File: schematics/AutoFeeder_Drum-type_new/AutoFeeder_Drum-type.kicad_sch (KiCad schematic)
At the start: 44 parts, among them J1 USB_C_Receptacle_6, J2 Conn_01x04, J3 Conn_01x05, J4 Conn_02x02_Odd_Even, J5 Conn_01x04, J6 Conn_02x02_Odd_Even, J7 Conn_01x04, J8 Conn_01x03, J9 Conn_01x04, M1 Motor_DC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

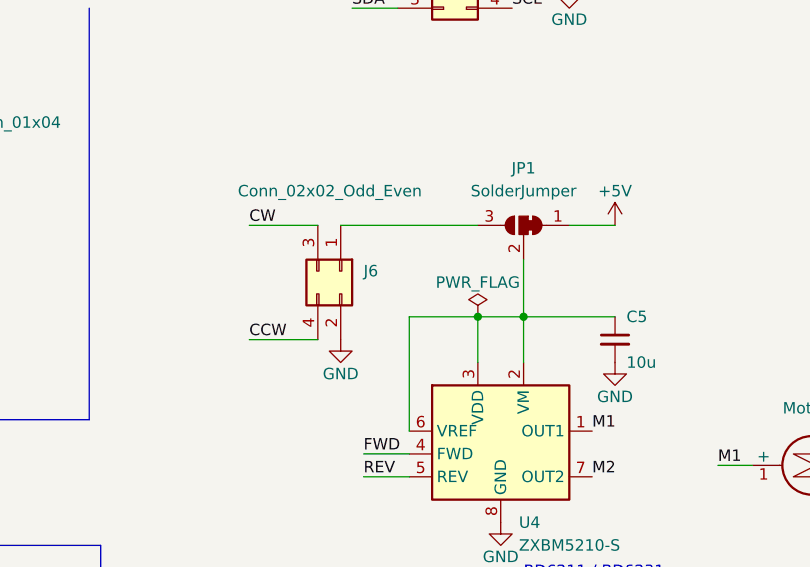
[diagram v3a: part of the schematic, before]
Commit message: Schematics: Add +5V to J6; Fine-tuning of patterns
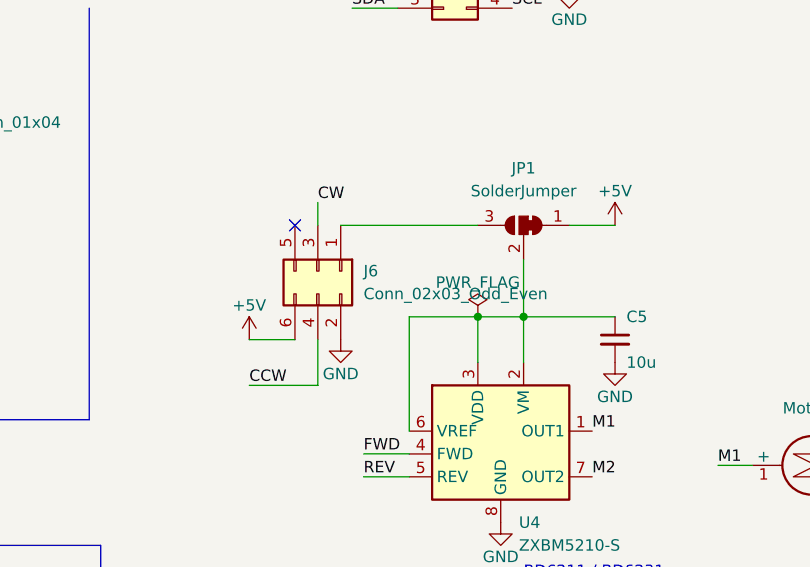
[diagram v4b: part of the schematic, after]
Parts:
- removed J6: Conn_02x02_Odd_Even, Connector_PinHeader_2.54mm:PinHeader_2x02_P2.54mm_Vertical, symbol Connector_Generic:Conn_02x02_Odd_Even
- added J6: Conn_02x03_Odd_Even, Connector_PinHeader_2.54mm:PinHeader_2x03_P2.54mm_Vertical, symbol Connector_Generic:Conn_02x03_Odd_Even
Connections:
- net +5V: now also J6.6 (Pin_6)
- net CCW: now also J6.4 (Pin_4)
- net CW: now also J6.3 (Pin_3)
- net GND: now also J6.2 (Pin_2)
- net at JP1.3 (B): now also J6.1 (Pin_1)
- no-connect marks 8 -> 9
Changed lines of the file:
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@@
   (no_connect (at 139.7 166.37))
   (no_connect (at 99.06 34.29))
+  (no_connect (at 193.04 121.92))
   (no_connect (at 118.11 26.67))
   (no_connect (at 99.06 39.37))
@@
     (stroke (width 0) (type default) (color 0 0 0 0))
   )
+  (wire (pts (xy 195.58 119.38) (xy 195.58 121.92))
+    (stroke (width 0) (type default) (color 0 0 0 0))
+  )
   (wire (pts (xy 228.6 121.92) (xy 223.52 121.92))
     (stroke (width 0) (type default) (color 0 0 0 0))
@@
     (stroke (width 0) (type default) (color 0 0 0 0))
   )
-  (wire (pts (xy 187.96 134.62) (xy 195.58 134.62))
+  (wire (pts (xy 187.96 139.7) (xy 195.58 139.7))
     (stroke (width 0) (type default) (color 0 0 0 0))
   )
@@
     (stroke (width 0) (type default) (color 0 0 0 0))
   )
+  (wire (pts (xy 195.58 134.62) (xy 195.58 139.7))
+    (stroke (width 0) (type default) (color 0 0 0 0))
+  )
   (wire (pts (xy 38.1 115.57) (xy 38.1 118.11))
     (stroke (width 0) (type default) (color 0 0 0 0))
@@
     (stroke (width 0) (type solid) (color 0 0 0 0))
   )
-  (wire (pts (xy 187.96 121.92) (xy 195.58 121.92))
-    (stroke (width 0) (type default) (color 0 0 0 0))
-  )
   (wire (pts (xy 198.12 72.39) (xy 205.74 72.39))
     (stroke (width 0) (type default) (color 0 0 0 0))
@@
   (polyline (pts (xy 90.17 62.23) (xy 91.44 59.69))
     (stroke (width 0) (type solid) (color 0 0 255 1))
+  )
+  (wire (pts (xy 187.96 134.62) (xy 193.04 134.62))
+    (stroke (width 0) (type default) (color 0 0 0 0))
   )
   (wire (pts (xy 38.1 118.11) (xy 43.18 118.11))
@@
     (effects (font (size 1.27 1.27)) (justify left bottom))
   )
-  (label "CW" (at 187.96 121.92 0)
+  (label "CW" (at 195.58 119.38 0)
     (effects (font (size 1.27 1.27)) (justify left bottom))
   )
@@
     (effects (font (size 1.27 1.27)) (justify left bottom))
   )
-  (label "CCW" (at 187.96 134.62 0)
+  (label "CCW" (at 187.96 139.7 0)
     (effects (font (size 1.27 1.27)) (justify left bottom))
   )
@@
   (label "Sensor0" (at 260.35 74.93 0)
     (effects (font (size 1.27 1.27)) (justify left bottom))
-  )
-  (symbol (lib_id "Connector_Generic:Conn_02x02_Odd_Even") (at 198.12 127 270) (unit 1)
-    (in_bom yes) (on_board yes)
-    (property "Reference" "J6" (id 0) (at 200.66 126.9999 90)
-      (effects (font (size 1.27 1.27)) (justify left))
-    )
-    (property "Value" "Conn_02x02_Odd_Even" (id 1) (at 186.69 118.11 90)
-      (effects (font (size 1.27 1.27)) (justify left))
-    )
-    (property "Footprint" "Connector_PinHeader_2.54mm:PinHeader_2x02_P2.54mm_Vertical" (id 2) (at 198.12 127 0)
-      (effects (font (size 1.27 1.27)) hide)
-    )
-    (property "Datasheet" "~" (id 3) (at 198.12 127 0)
-      (effects (font (size 1.27 1.27)) hide)
-    )
-    (pin "1")
-    (pin "2")
-    (pin "3")
-    (pin "4")
   )
   (symbol (lib_id "Device:R") (at 107.95 105.41 270) (unit 1)
@@
     (pin "1")
   )
-  (symbol (lib_id "mylib1:SW_PUSH_DPDT_x2") (at 251.46 64.77 0) (unit 2)
-    (in_bom yes) (on_board yes) (fields_autoplaced)
-    (property "Reference" "SW3" (id 0) (at 251.46 57.15 0))
-    (property "Value" "IS-2235" (id 1) (at 251.46 59.69 0))
-    (property "Footprint" "mylib:Slide-SW-IS-2235" (id 2) (at 251.46 64.77 0)
-      (effects (font (size 1.27 1.27)) hide)
-    )
-    (property "Datasheet" "" (id 3) (at 251.46 64.77 0)
+  (symbol (lib_id "Connector_Generic:Conn_02x03_Odd_Even") (at 195.58 127 270) (unit 1)
+    (in_bom yes) (on_board yes) (fields_autoplaced)
+    (property "Reference" "J6" (id 0) (at 200.66 126.9999 90)
+      (effects (font (size 1.27 1.27)) (justify left))
+    )
+    (property "Value" "Conn_02x03_Odd_Even" (id 1) (at 200.66 129.5399 90)
+      (effects (font (size 1.27 1.27)) (justify left))
+    )
+    (property "Footprint" "Connector_PinHeader_2.54mm:PinHeader_2x03_P2.54mm_Vertical" (id 2) (at 195.58 127 0)
+      (effects (font (size 1.27 1.27)) hide)
+    )
+    (property "Datasheet" "~" (id 3) (at 195.58 127 0)
       (effects (font (size 1.27 1.27)) hide)
     )
@@
     (pin "6")
   )
-  (symbol (lib_id "mylib1:SW_PUSH_DPDT_x2") (at 123.19 36.83 0) (mirror y) (unit 1)
-    (in_bom yes) (on_board yes) (fields_autoplaced)
-    (property "Reference" "SW2" (id 0) (at 123.19 29.21 0))
-    (property "Value" "IS-2235" (id 1) (at 123.19 31.75 0))
-    (property "Footprint" "mylib:Slide-SW-IS-2235" (id 2) (at 123.19 36.83 0)
-      (effects (font (size 1.27 1.27)) hide)
-    )
-    (property "Datasheet" "" (id 3) (at 123.19 36.83 0)
+  (symbol (lib_id "mylib1:SW_PUSH_DPDT_x2") (at 251.46 64.77 0) (unit 2)
+    (in_bom yes) (on_board yes) (fields_autoplaced)
+    (property "Reference" "SW3" (id 0) (at 251.46 57.15 0))
+    (property "Value" "IS-2235" (id 1) (at 251.46 59.69 0))
+    (property "Footprint" "mylib:Slide-SW-IS-2235" (id 2) (at 251.46 64.77 0)
+      (effects (font (size 1.27 1.27)) hide)
+    )
+    (property "Datasheet" "" (id 3) (at 251.46 64.77 0)
       (effects (font (size 1.27 1.27)) hide)
     )
@@
     (pin "6")
   )
+  (symbol (lib_id "mylib1:SW_PUSH_DPDT_x2") (at 123.19 36.83 0) (mirror y) (unit 1)
+    (in_bom yes) (on_board yes) (fields_autoplaced)
+    (property "Reference" "SW2" (id 0) (at 123.19 29.21 0))
+    (property "Value" "IS-2235" (id 1) (at 123.19 31.75 0))
+    (property "Footprint" "mylib:Slide-SW-IS-2235" (id 2) (at 123.19 36.83 0)
+      (effects (font (size 1.27 1.27)) hide)
+    )
+    (property "Datasheet" "" (id 3) (at 123.19 36.83 0)
+      (effects (font (size 1.27 1.27)) hide)
+    )
+    (pin "1")
+    (pin "2")
+    (pin "3")
+    (pin "4")
+    (pin "5")
+    (pin "6")
+  )
   (symbol (lib_id "Device:R") (at 100.33 180.34 0) (unit 1)
     (in_bom yes) (on_board yes)
@@
     )
     (property "Datasheet" "~" (id 3) (at 43.18 118.11 0)
+      (effects (font (size 1.27 1.27)) hide)
+    )
+    (pin "1")
+  )
+  (symbol (lib_id "power:+5V") (at 187.96 134.62 0) (unit 1)
+    (in_bom yes) (on_board yes)
+    (property "Reference" "#PWR032" (id 0) (at 187.96 138.43 0)
+      (effects (font (size 1.27 1.27)) hide)
+    )
+    (property "Value" "+5V" (id 1) (at 187.96 130.81 0))
+    (property "Footprint" "" (id 2) (at 187.96 134.62 0)
+      (effects (font (size 1.27 1.27)) hide)
+    )
+    (property "Datasheet" "" (id 3) (at 187.96 134.62 0)
       (effects (font (size 1.27 1.27)) hide)
     )
@@
       (reference "#PWR031") (unit 1) (value "GND") (footprint "")
     )
+    (path "/7284a21b-ce4a-4b5d-b841-362f0fe9fe46"
+      (reference "#PWR032") (unit 1) (value "+5V") (footprint "")
+    )
     (path "/acf7ad7b-448c-4d5e-b918-6629b97c5c52"
       (reference "#PWR0101") (unit 1) (value "GND") (footprint "")
@@
       (reference "J5") (unit 1) (value "Conn_01x04") (footprint "Connector_PinHeader_2.54mm:PinHeader_1x04_P2.54mm_Vertical")
     )
-    (path "/06161094-4bc5-40fc-8876-0dc0fd47eb89"
-      (reference "J6") (unit 1) (value "Conn_02x02_Odd_Even") (footprint "Connector_PinHeader_2.54mm:PinHeader_2x02_P2.54mm_Vertical")
+    (path "/3fed5ca2-676a-417e-8da5-f194c57c4985"
+      (reference "J6") (unit 1) (value "Conn_02x03_Odd_Even") (footprint "Connector_PinHeader_2.54mm:PinHeader_2x03_P2.54mm_Vertical")
     )
     (path "/b635d2c1-9675-4c71-b0c4-4bae6007c9fe"

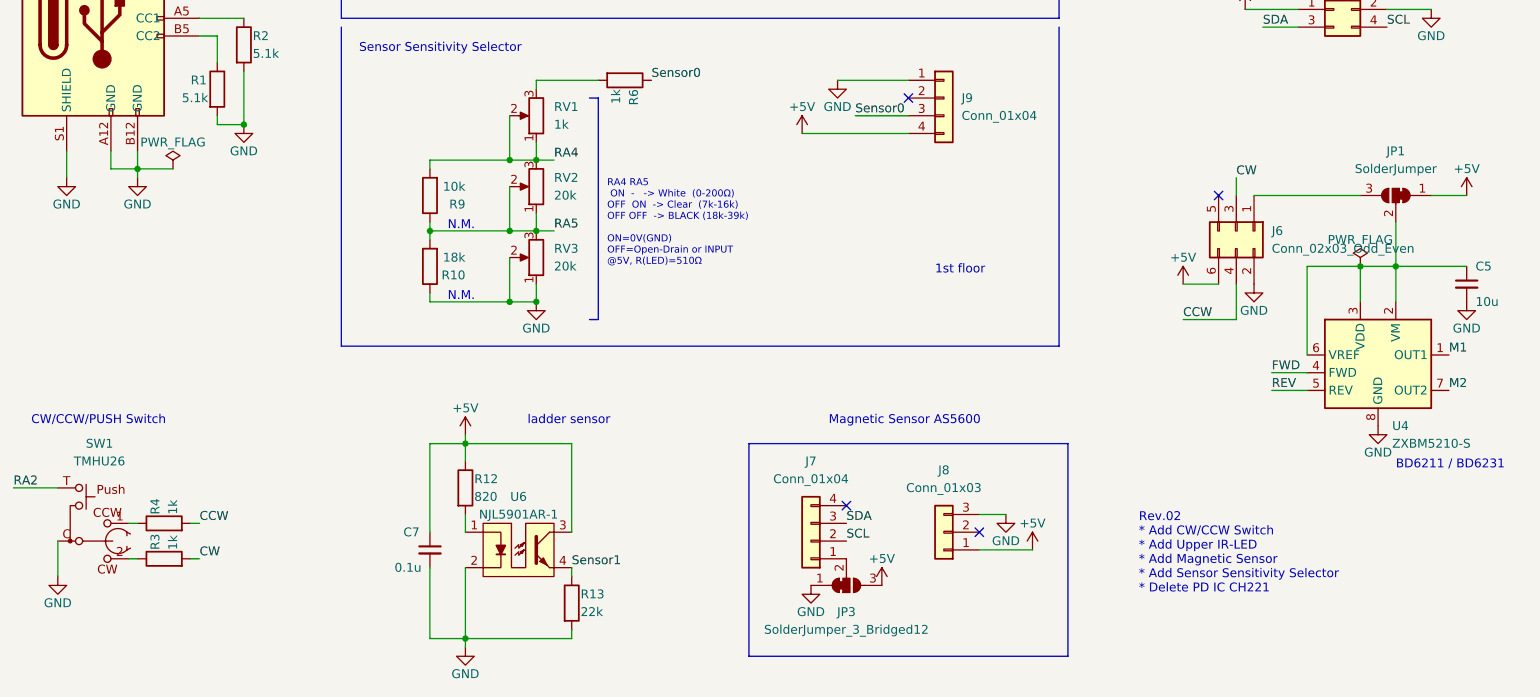
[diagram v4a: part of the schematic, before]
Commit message: Schematics: Add Diode OR (D3 and D4) for manual feed and auto feed
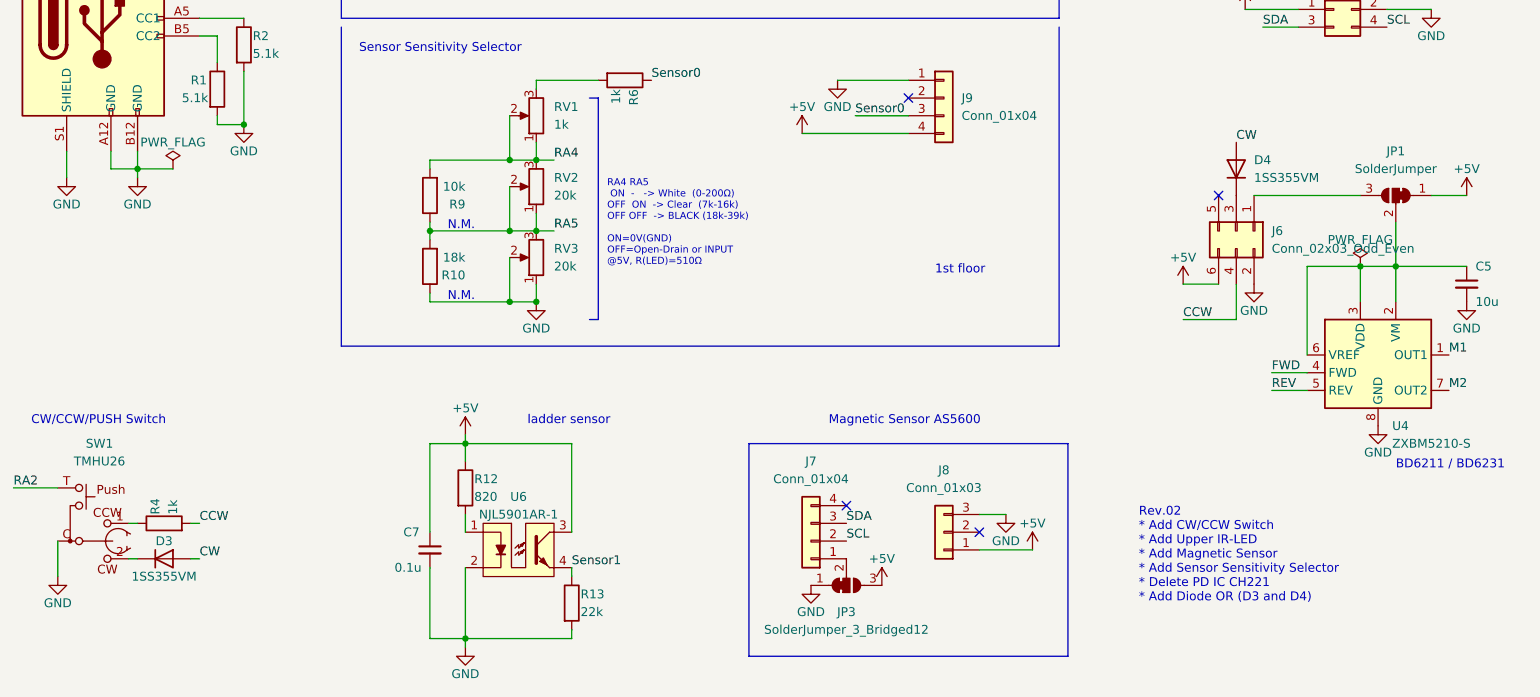
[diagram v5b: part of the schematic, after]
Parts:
- removed R3: 1k, Resistor_SMD:R_0603_1608Metric, symbol Device:R
- added D3, D4: 1SS355VM, Diode_SMD:D_SOD-323F, symbol Diode:1SS355VM
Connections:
- net CW: now also D3.2 (A), D4.2 (A); no longer J6.3 (Pin_3)
- net at SW1.2: now also D3.1 (K)
- new net: D4.1 (K), J6.3 (Pin_3)
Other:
- note added: "Rev.02 * Add CW/CCW Switch * Add Upper IR-LED * Add Magnetic Sensor * Add Sensor Sensitivity Selector * Delete PD IC CH221 * Add Diode OR (D3 and D4)"
- note removed: "Rev.02 * Add CW/CCW Switch * Add Upper IR-LED * Add Magnetic Sensor * Add Sensor Sensitivity Selector * Delete PD IC CH221"
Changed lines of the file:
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@@
-    (stroke (width 0) (type default) (color 0 0 0 0))
-  )
-  (wire (pts (xy 195.58 119.38) (xy 195.58 121.92))
     (stroke (width 0) (type default) (color 0 0 0 0))
   )
@@
     (effects (font (size 1.27 1.27)) (justify left bottom))
   )
-  (text "Rev.02\n* Add CW/CCW Switch\n* Add Upper IR-LED\n* Add Magnetic Sensor\n* Add Sensor Sensitivity Selector\n* Delete PD IC CH221\n"
-    (at 181.61 179.07 0)
+  (text "Rev.02\n* Add CW/CCW Switch\n* Add Upper IR-LED\n* Add Magnetic Sensor\n* Add Sensor Sensitivity Selector\n* Delete PD IC CH221\n* Add Diode OR (D3 and D4)\n"
+    (at 181.61 180.34 0)
     (effects (font (size 1.27 1.27)) (justify left bottom))
   )
@@
     (effects (font (size 1.27 1.27)) (justify left bottom))
   )
-  (label "CW" (at 195.58 119.38 0)
+  (label "CW" (at 195.58 114.3 0)
     (effects (font (size 1.27 1.27)) (justify left bottom))
   )
@@
     (pin "1")
   )
+  (symbol (lib_id "Diode:1SS355VM") (at 195.58 118.11 90) (unit 1)
+    (in_bom yes) (on_board yes) (fields_autoplaced)
+    (property "Reference" "D4" (id 0) (at 198.12 116.8399 90)
+      (effects (font (size 1.27 1.27)) (justify right))
+    )
+    (property "Value" "1SS355VM" (id 1) (at 198.12 119.3799 90)
+      (effects (font (size 1.27 1.27)) (justify right))
+    )
+    (property "Footprint" "Diode_SMD:D_SOD-323F" (id 2) (at 200.025 118.11 0)
+      (effects (font (size 1.27 1.27)) hide)
+    )
+    (property "Datasheet" "https://fscdn.rohm.com/en/products/databook/datasheet/discrete/diode/switching/1ss355vmte-17-e.pdf" (id 3) (at 195.58 118.11 0)
+      (effects (font (size 1.27 1.27)) hide)
+    )
+    (pin "1")
+    (pin "2")
+  )
   (symbol (lib_id "Device:C_Small") (at 201.93 57.15 0) (unit 1)
     (in_bom yes) (on_board yes)
@@
     )
     (property "Datasheet" "~" (id 3) (at 256.54 46.99 0)
-      (effects (font (size 1.27 1.27)) hide)
-    )
-    (pin "1")
-    (pin "2")
-  )
-  (symbol (lib_id "Device:R") (at 41.91 173.99 90) (unit 1)
-    (in_bom yes) (on_board yes)
-    (property "Reference" "R3" (id 0) (at 40.64 172.72 0)
-      (effects (font (size 1.27 1.27)) (justify left))
-    )
-    (property "Value" "1k" (id 1) (at 43.18 172.72 0)
-      (effects (font (size 1.27 1.27)) (justify left))
-    )
-    (property "Footprint" "Resistor_SMD:R_0603_1608Metric" (id 2) (at 41.91 175.768 90)
-      (effects (font (size 1.27 1.27)) hide)
-    )
-    (property "Datasheet" "~" (id 3) (at 41.91 173.99 0)
       (effects (font (size 1.27 1.27)) hide)
     )
@@
     (pin "3")
     (pin "4")
+  )
+  (symbol (lib_id "Diode:1SS355VM") (at 41.91 173.99 0) (unit 1)
+    (in_bom yes) (on_board yes)
+    (property "Reference" "D3" (id 0) (at 41.91 171.45 0))
+    (property "Value" "1SS355VM" (id 1) (at 41.91 176.53 0))
+    (property "Footprint" "Diode_SMD:D_SOD-323F" (id 2) (at 41.91 178.435 0)
+      (effects (font (size 1.27 1.27)) hide)
+    )
+    (property "Datasheet" "https://fscdn.rohm.com/en/products/databook/datasheet/discrete/diode/switching/1ss355vmte-17-e.pdf" (id 3) (at 41.91 173.99 0)
+      (effects (font (size 1.27 1.27)) hide)
+    )
+    (pin "1")
+    (pin "2")
   )
   (symbol (lib_id "Device:C_Small") (at 133.35 82.55 0) (unit 1)
@@
       (reference "D2") (unit 1) (value "LED") (footprint "LED_SMD:LED_0603_1608Metric")
     )
+    (path "/f0db48d2-10f2-44f8-9e5d-5a34b783b58e"
+      (reference "D3") (unit 1) (value "1SS355VM") (footprint "Diode_SMD:D_SOD-323F")
+    )
+    (path "/28b95d4e-f025-4173-8e6a-7b5e4ef45717"
+      (reference "D4") (unit 1) (value "1SS355VM") (footprint "Diode_SMD:D_SOD-323F")
+    )
     (path "/f74a052d-f40a-4ac4-9842-a16dfd9c259b"
       (reference "J1") (unit 1) (value "USB_C_Receptacle_6") (footprint "mylib:USB_C_6")
@@
       (reference "R2") (unit 1) (value "5.1k") (footprint "Resistor_SMD:R_0603_1608Metric")
     )
-    (path "/b4115d81-b868-487b-aa67-bef8491b5649"
-      (reference "R3") (unit 1) (value "1k") (footprint "Resistor_SMD:R_0603_1608Metric")
-    )
     (path "/a583dddb-ff3b-4ea5-86bb-ba6d25742e1f"

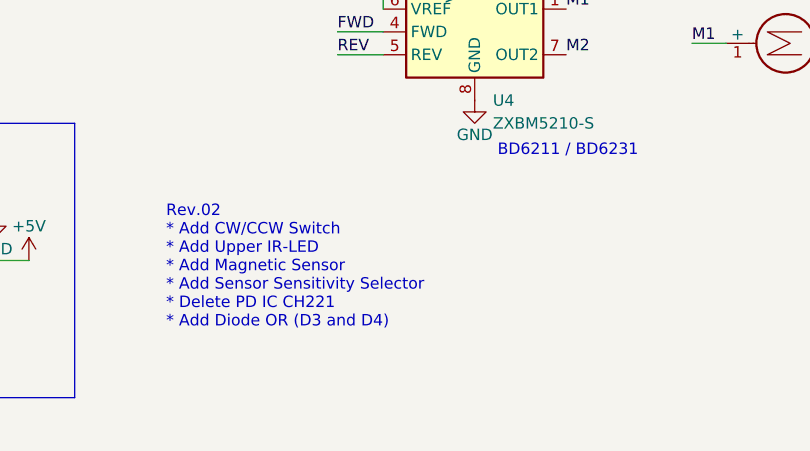
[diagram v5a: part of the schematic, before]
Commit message: Change the position of M3 mounting hole / Add silk printing of magnetic sensor / Add Diode OR (D3,D4) to allow advancing one component either by manual switch or automatic control / Slightly modified pattern routing. Completed as Rev.02 board
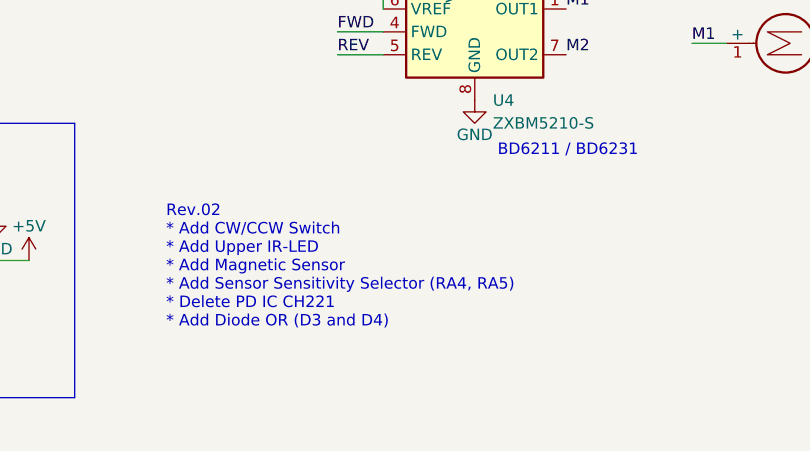
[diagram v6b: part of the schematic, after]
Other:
- note added: "Rev.02 * Add CW/CCW Switch * Add Upper IR-LED * Add Magnetic Sensor * Add Sensor Sensitivity Selector (RA4, RA5) * Delete PD IC CH221 * Add Diode OR (D3 and D4)"
- note removed: "Rev.02 * Add CW/CCW Switch * Add Upper IR-LED * Add Magnetic Sensor * Add Sensor Sensitivity Selector * Delete PD IC CH221 * Add Diode OR (D3 and D4)"
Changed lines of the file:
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@@
     (effects (font (size 1.27 1.27)) (justify left bottom))
   )
-  (text "Rev.02\n* Add CW/CCW Switch\n* Add Upper IR-LED\n* Add Magnetic Sensor\n* Add Sensor Sensitivity Selector\n* Delete PD IC CH221\n* Add Diode OR (D3 and D4)\n"
+  (text "Rev.02\n* Add CW/CCW Switch\n* Add Upper IR-LED\n* Add Magnetic Sensor\n* Add Sensor Sensitivity Selector (RA4, RA5)\n* Delete PD IC CH221\n* Add Diode OR (D3 and D4)\n"
     (at 181.61 180.34 0)
     (effects (font (size 1.27 1.27)) (justify left bottom))
